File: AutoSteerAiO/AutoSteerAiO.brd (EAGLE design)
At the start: 114.3 x 99.1 mm, 88 parts, among them K4 CB1A-P-12V, U1 VX7805-1000

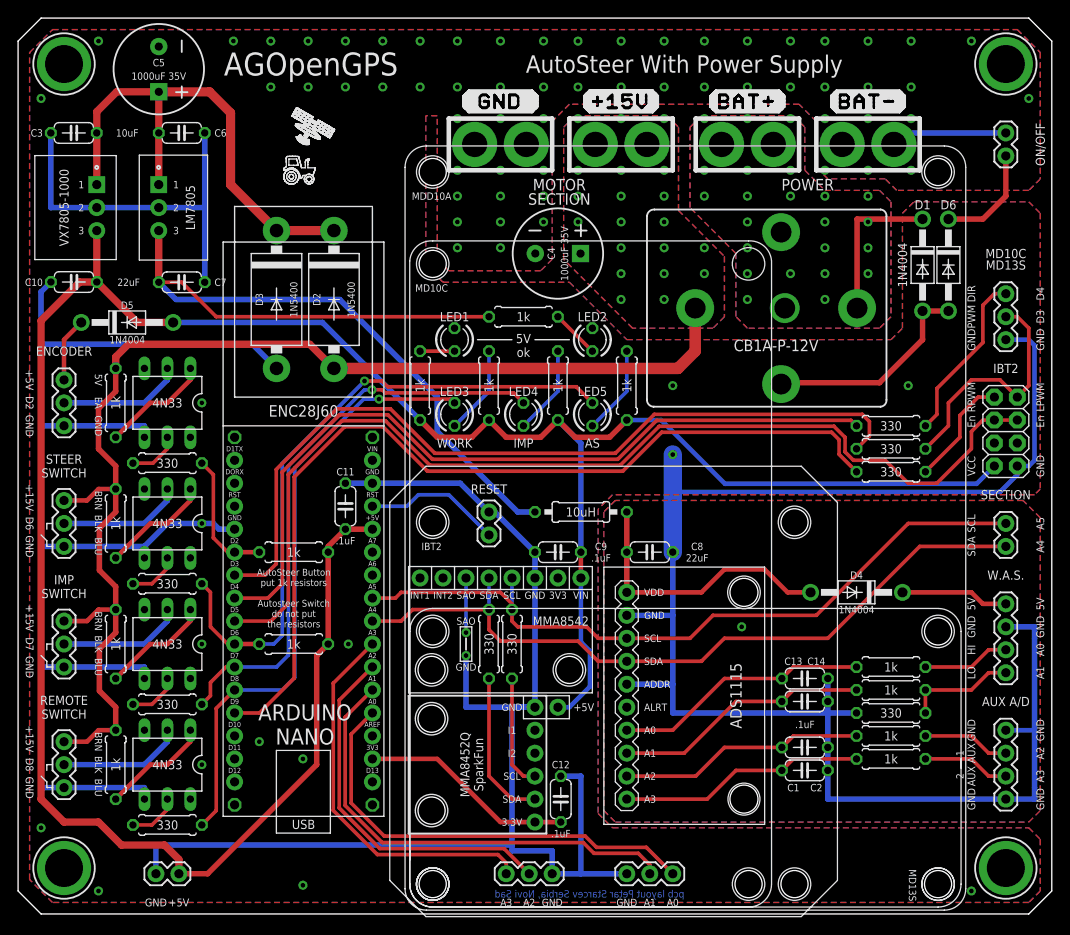
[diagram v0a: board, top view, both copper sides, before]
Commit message: Add files via upload
replaced VX7805-500 with LM7805 - power supply for W.A.S.
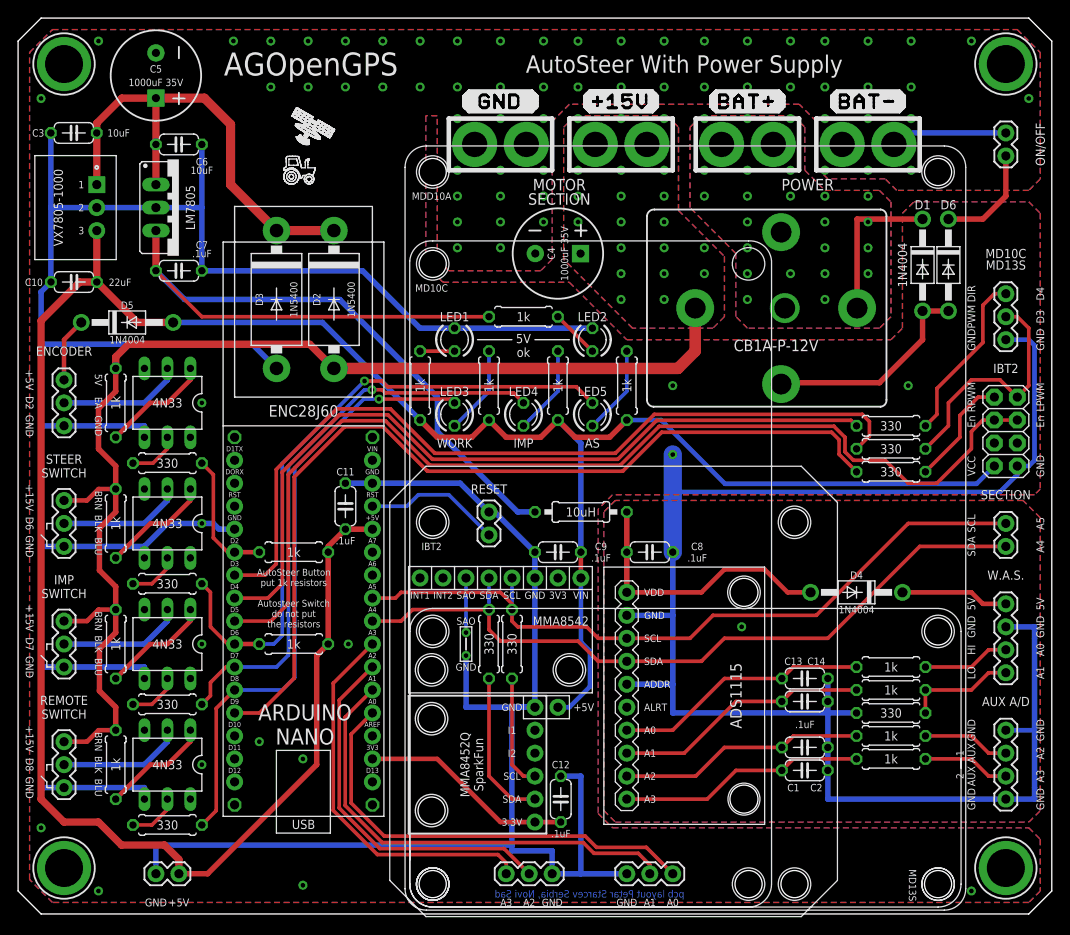
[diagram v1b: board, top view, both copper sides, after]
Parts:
- removed PS1: VX7805-500, #VX7805-500:VX7805500
- added IC1: (no value), v-reg:78XXS
- C7, C8: value 22uF -> .1uF
- moved C7 1.31 mm to (17.8, 71.1)
- moved C6 1.31 mm to (17.8, 85.1)
- moved C5 0.77 mm to (15.2, 92.7)
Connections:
- net GND: now also IC1.GND; no longer PS1.2
- net N$25: now also IC1.OUT; no longer PS1.3
- net N$26: now also IC1.IN; no longer PS1.1
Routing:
- net GND: track 559.5 -> 610.7 mm
- net N$26: track 56.5 -> 53.7 mm

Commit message: Add files via upload
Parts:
- moved C12 0.95 mm to (61.0, 12.7)
- moved C8 0.63 mm to (69.8, 40.6)
- moved C9 0.63 mm to (59.7, 40.6)
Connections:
- net N$21 renamed A+5V.
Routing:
- net GND: track 610.7 -> 645.3 mm, vias 79 -> 78
- net +3V3: track 23.7 -> 24.7 mm

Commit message: Add files via upload
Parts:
- added C15: .1uF, resistor:C050-024X044
- renumbered IC1 to 7805
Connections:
- net GND: now also C15.1
- net N$25: now also C15.2
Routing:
- net GND: track 645.3 -> 628.1 mm, vias 78 -> 80
- net N$25: track 98.6 -> 100.8 mm
